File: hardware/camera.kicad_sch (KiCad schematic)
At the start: 4 parts, among them J1 RS2-18-G, Q4 DMN1008UFDF-7

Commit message: Done?
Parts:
- R19: footprint Resistor_SMD:R_0603_1608Metric -> Resistor_SMD:R_0402_1005Metric
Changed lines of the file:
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@@
 			)
 		)
-		(property "Footprint" "Resistor_SMD:R_0603_1608Metric"
+		(property "Footprint" "Resistor_SMD:R_0402_1005Metric"
 			(at 101.092 38.1 90)
 			(effects

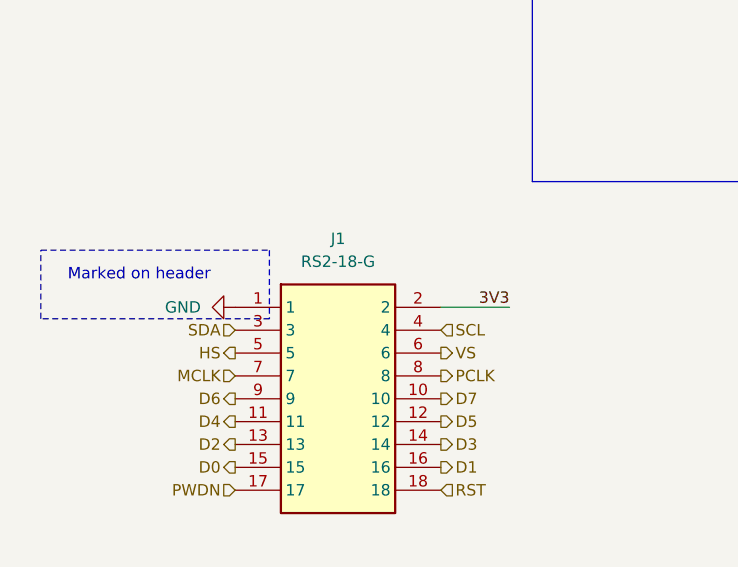
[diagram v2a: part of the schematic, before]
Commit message: Fixed MOS and board connector
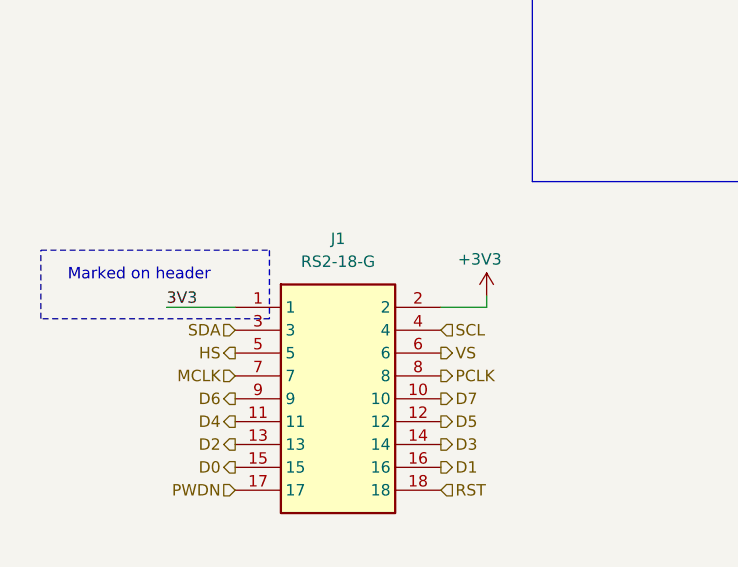
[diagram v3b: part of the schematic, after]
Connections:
- net 3V3: now also J1.1; no longer J1.2
- net GND: no longer J1.1
- new net +3V3: J1.2
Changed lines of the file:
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@@
+	(wire
+		(pts
+			(xy 64.77 76.2) (xy 64.77 77.47)
+		)
+		(stroke
+			(width 0)
+			(type default)
+		)
+	)
 	(wire
 		(pts
@@
 	(wire
 		(pts
+			(xy 29.21 77.47) (xy 36.83 77.47)
+		)
+		(stroke
+			(width 0)
+			(type default)
+		)
+	)
+	(wire
+		(pts
 			(xy 102.87 41.91) (xy 102.87 44.45)
 		)
@@
 	(wire
 		(pts
-			(xy 59.69 77.47) (xy 67.31 77.47)
-		)
-		(stroke
-			(width 0)
-			(type default)
-		)
-	)
-	(wire
-		(pts
 			(xy 172.72 30.48) (xy 173.99 30.48)
 		)
@@
 		(pts
 			(xy 172.72 27.94) (xy 173.99 27.94)
+		)
+		(stroke
+			(width 0)
+			(type default)
+		)
+	)
+	(wire
+		(pts
+			(xy 64.77 77.47) (xy 59.69 77.47)
 		)
 		(stroke
@@
 	)
 	(label "3V3"
-		(at 67.31 77.47 180)
-		(effects
-			(font
-				(size 1.27 1.27)
-			)
-			(justify right bottom)
+		(at 29.21 77.47 0)
+		(effects
+			(font
+				(size 1.27 1.27)
+			)
+			(justify left bottom)
 		)
 	)
@@
 	(symbol
 		(lib_id "power:GND")
-		(at 36.83 77.47 270)
-		(mirror x)
-		(unit 1)
-		(exclude_from_sim no)
-		(in_bom yes)
-		(on_board yes)
-		(dnp no)
-		(fields_autoplaced yes)
-		(property "Reference" "#PWR021"
-			(at 30.48 77.47 0)
-			(effects
-				(font
-					(size 1.27 1.27)
-				)
-				(hide yes)
-			)
-		)
-		(property "Value" "GND"
-			(at 33.02 77.4699 90)
-			(effects
-				(font
-					(size 1.27 1.27)
-				)
-				(justify right)
-			)
-		)
-		(property "Footprint" ""
-			(at 36.83 77.47 0)
-			(effects
-				(font
-					(size 1.27 1.27)
-				)
-				(hide yes)
-			)
-		)
-		(property "Datasheet" ""
-			(at 36.83 77.47 0)
-			(effects
-				(font
-					(size 1.27 1.27)
-				)
-				(hide yes)
-			)
-		)
-		(property "Description" "Power symbol creates a global label with name \"GND\" , ground"
-			(at 36.83 77.47 0)
-			(effects
-				(font
-					(size 1.27 1.27)
-				)
-				(hide yes)
-			)
-		)
-		(pin "1"
-		)
-		(instances
-			(project ""
-				(path "/e8e834c4-1afb-42f7-b718-3cb720dae1d5/a0c7114d-8344-4dfb-8086-bd9d063d8594"
-					(reference "#PWR021")
-					(unit 1)
-				)
-			)
-		)
-	)
-	(symbol
-		(lib_id "power:GND")
 		(at 134.62 33.02 270)
 		(unit 1)
@@
 					(unit 1)
 				)
+			)
+		)
+	)
+	(symbol
+		(lib_id "power:+3V3")
+		(at 64.77 76.2 0)
+		(unit 1)
+		(exclude_from_sim no)
+		(in_bom yes)
+		(on_board yes)
+		(dnp no)
+		(property "Reference" "#PWR021"
+			(at 64.77 80.01 0)
+			(effects
+				(font
+					(size 1.27 1.27)
+				)
+				(hide yes)
+			)
+		)
+		(property "Value" "+3V3"
+			(at 64.008 72.136 0)
+			(effects
+				(font
+					(size 1.27 1.27)
+				)
+			)
+		)
+		(property "Footprint" ""
+			(at 64.77 76.2 0)
+			(effects
+				(font
+					(size 1.27 1.27)
+				)
+				(hide yes)
+			)
+		)
+		(property "Datasheet" ""
+			(at 64.77 76.2 0)
+			(effects
+				(font
+					(size 1.27 1.27)
+				)
+				(hide yes)
+			)
+		)
+		(property "Description" "Power symbol creates a global label with name \"+3V3\""
+			(at 64.77 76.2 0)
+			(effects
+				(font
+					(size 1.27 1.27)
+				)
+				(hide yes)
+			)
+		)
+		(pin "1"
+		)
+		(instances
+			(project "obvod"
+				(path "/e8e834c4-1afb-42f7-b718-3cb720dae1d5/a0c7114d-8344-4dfb-8086-bd9d063d8594"
+					(reference "#PWR021")
+					(unit 1)
+				)

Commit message: Revised and completed BOM
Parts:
- renumbered J1 to J4, Q4 to Q5, R19 to R21, R20 to R22
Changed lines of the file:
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@@
 		(dnp no)
 		(fields_autoplaced yes)
-		(property "Reference" "Q4"
+		(property "Reference" "Q5"
 			(at 153.67 17.78 0)
 			(effects
@@
 			(project ""
 				(path "/e8e834c4-1afb-42f7-b718-3cb720dae1d5/a0c7114d-8344-4dfb-8086-bd9d063d8594"
-					(reference "Q4")
+					(reference "Q5")
 					(unit 1)
 				)
@@
 		(dnp no)
 		(fields_autoplaced yes)
-		(property "Reference" "R19"
+		(property "Reference" "R21"
 			(at 105.41 36.8299 0)
 			(effects
@@
 			(project ""
 				(path "/e8e834c4-1afb-42f7-b718-3cb720dae1d5/a0c7114d-8344-4dfb-8086-bd9d063d8594"
-					(reference "R19")
+					(reference "R21")
 					(unit 1)
 				)
@@
 		(on_board yes)
 		(dnp no)
-		(property "Reference" "R20"
+		(property "Reference" "R22"
 			(at 118.11 25.4 90)
 			(effects
@@
 			(project "obvod"
 				(path "/e8e834c4-1afb-42f7-b718-3cb720dae1d5/a0c7114d-8344-4dfb-8086-bd9d063d8594"
-					(reference "R20")
+					(reference "R22")
 					(unit 1)
 				)
@@
 		(dnp no)
 		(fields_autoplaced yes)
-		(property "Reference" "J1"
+		(property "Reference" "J4"
 			(at 48.26 69.85 0)
 			(effects
@@
 			(project ""
 				(path "/e8e834c4-1afb-42f7-b718-3cb720dae1d5/a0c7114d-8344-4dfb-8086-bd9d063d8594"
-					(reference "J1")
-					(unit 1)
-				)
+					(reference "J4")
+					(unit 1)
+				)
